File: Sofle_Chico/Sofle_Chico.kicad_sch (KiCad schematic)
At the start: 114 parts, among them J1 Conn_01x05, J2 MJ-4PP-9, J3 Conn_01x04, J4 Conn_01x04, J5 Conn_01x05, J6 Conn_01x05, J7 Conn_01x04, Q1 DMG2305UX, SW1 SW_PUSH, SW10 SW_PUSH, SW11 SW_PUSH, SW12 SW_PUSH, SW13 SW_PUSH, SW14 SW_PUSH, SW15 SW_PUSH, SW16 SW_PUSH, SW17 SW_PUSH, SW18 SW_PUSH, SW19 SW_PUSH, SW2 SW_PUSH, SW20 SW_PUSH, SW21 SW_PUSH, SW22 SW_PUSH, SW23 SW_PUSH, SW24 SW_PUSH, SW25 Rotary_Encoder_Switch-Device, SW26 SW_PUSH, SW27 SW_PUSH, SW28 SW_PUSH, SW29 SW_PUSH, SW3 SW_PUSH, SW30 SW_PUSH, SW4 SW_PUSH, SW5 SW_PUSH, SW6 SW_PUSH, SW7 SW_PUSH, SW8 SW_PUSH, SW9 SW_PUSH, U1 SN74AHCT1G125, U2 Pico

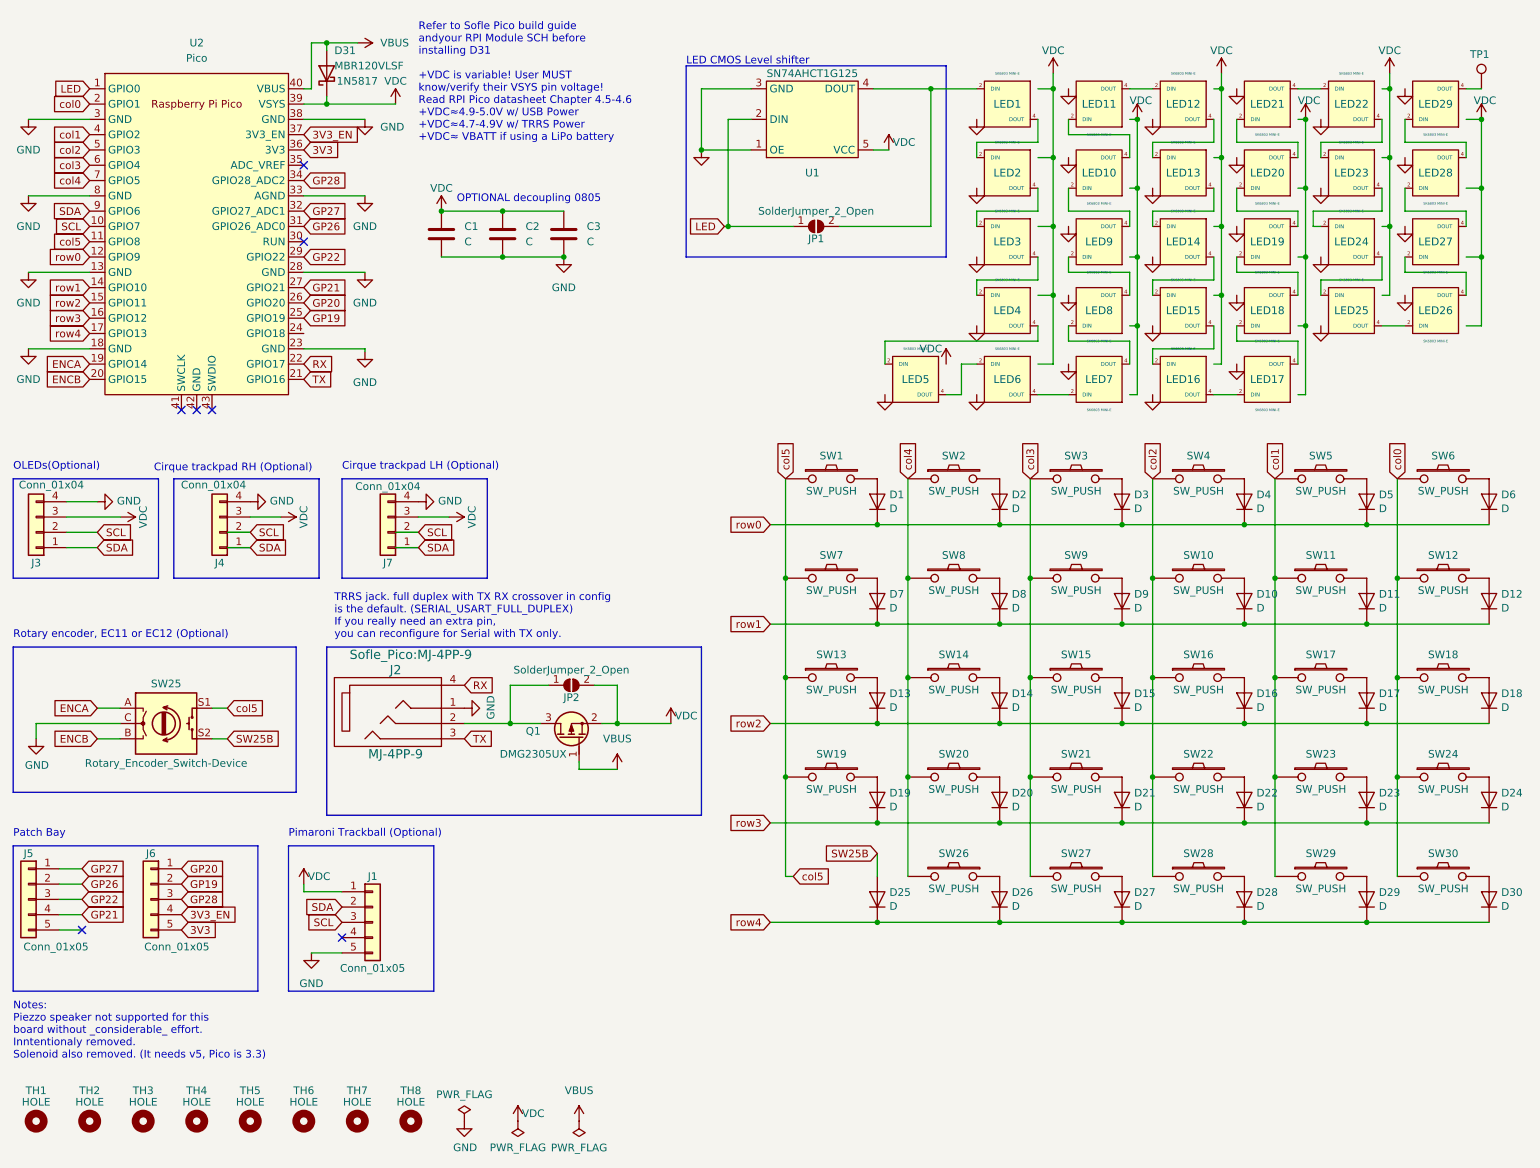
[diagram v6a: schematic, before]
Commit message: Completed routing and teardrops and cleared essential DRC errors
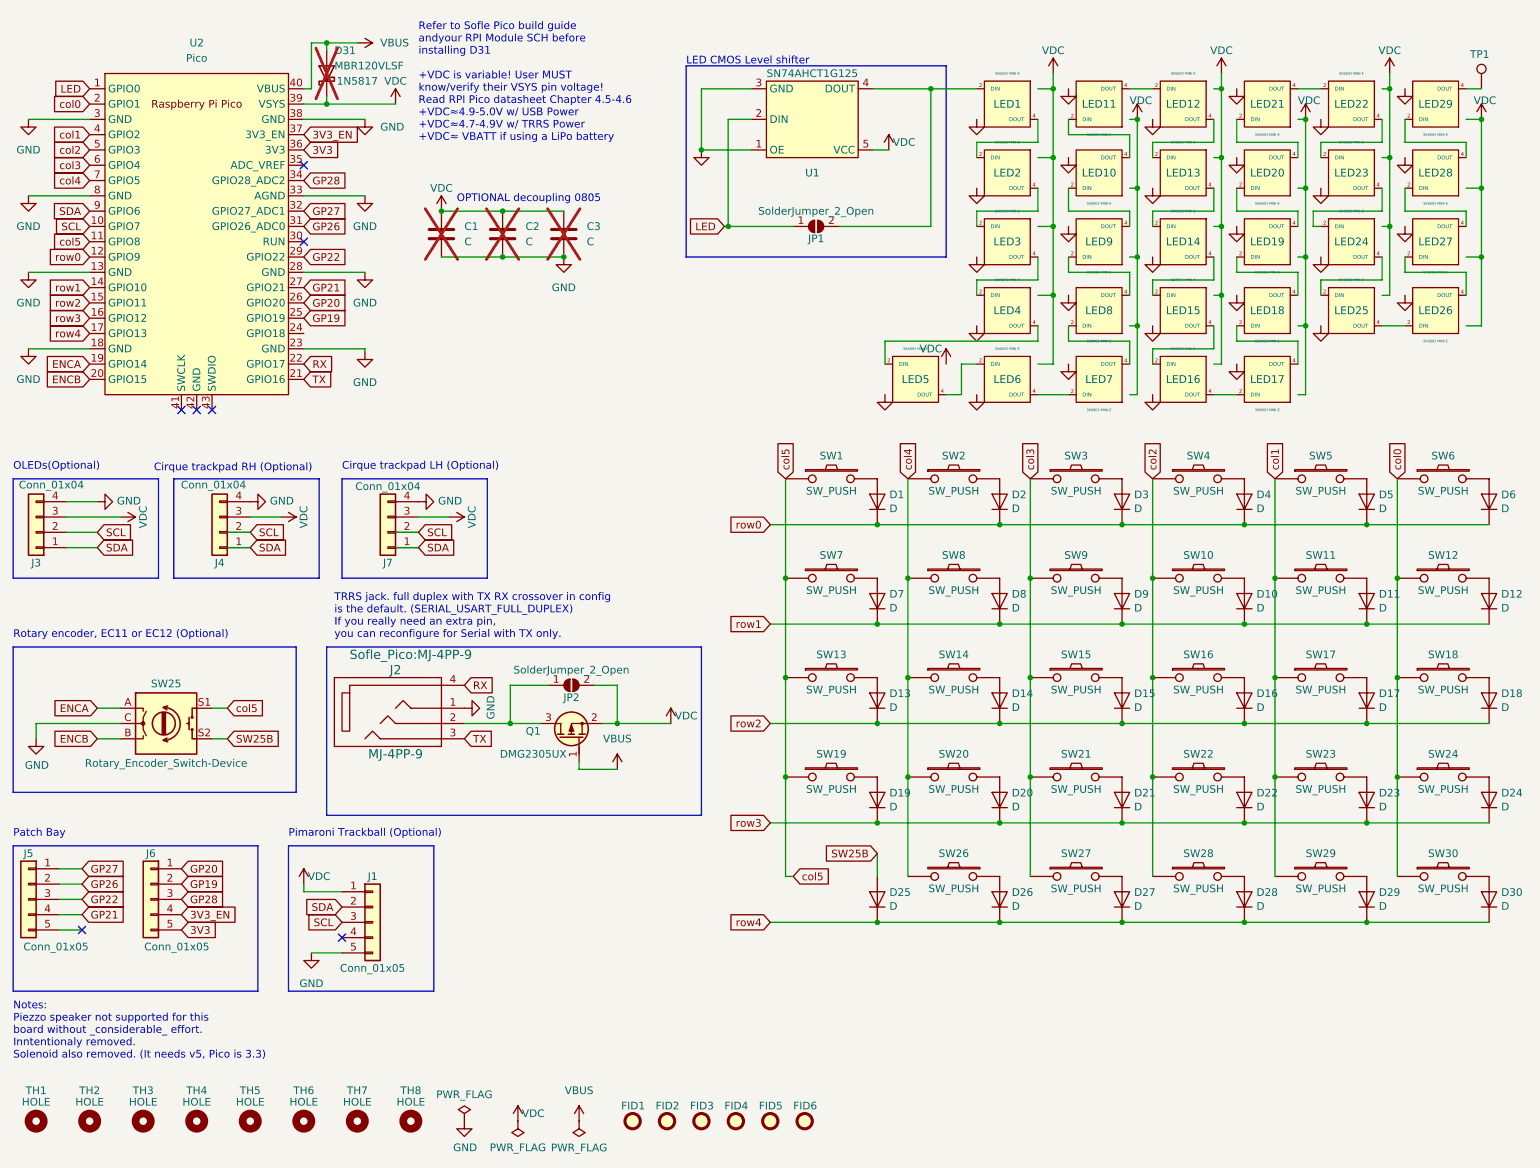
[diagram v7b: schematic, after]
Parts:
- added FID1, FID2, FID3, FID4, FID5, FID6: Fiducial, Fiducial:Fiducial_0.5mm_Mask1.5mm, symbol Mechanical:Fiducial
- C1, C2, C3, D31: now not fitted
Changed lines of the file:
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@@
+    )
+  )
+  (symbol (lib_id "Mechanical:Fiducial") (at 123.825 196.85 0) (unit 1)
+    (in_bom yes) (on_board yes) (dnp no)
+    (property "Reference" "FID2" (at 121.92 194.31 0)
+      (effects (font (size 1.27 1.27)) (justify left))
+    )
+    (property "Value" "Fiducial" (at 125.984 198.0621 0)
+      (effects (font (size 1.27 1.27)) (justify left) hide)
+    )
+    (property "Footprint" "Fiducial:Fiducial_0.5mm_Mask1.5mm" (at 123.825 196.85 0)
+      (effects (font (size 1.27 1.27)) hide)
+    )
+    (property "Datasheet" "~" (at 123.825 196.85 0)
+      (effects (font (size 1.27 1.27)) hide)
+    )
+    (instances
+      (project "Sofle_Chico"
+        (path "/06057b3a-55ab-4f4e-913e-2aeec5ff3587"
+          (reference "FID2") (unit 1)
+        )
+      )
     )
   )
@@
   )
   (symbol (lib_id "Device:C") (at 106.68 49.53 0) (unit 1)
-    (in_bom yes) (on_board yes) (dnp no) (fields_autoplaced)
+    (in_bom yes) (on_board yes) (dnp yes)
     (property "Reference" "C3" (at 110.49 48.26 0)
       (effects (font (size 1.27 1.27)) (justify left))
@@
         (path "/06057b3a-55ab-4f4e-913e-2aeec5ff3587"
           (reference "#PWR0113") (unit 1)
+        )
+      )
+    )
+  )
+  (symbol (lib_id "Mechanical:Fiducial") (at 146.685 196.85 0) (unit 1)
+    (in_bom yes) (on_board yes) (dnp no)
+    (property "Reference" "FID6" (at 144.78 194.31 0)
+      (effects (font (size 1.27 1.27)) (justify left))
+    )
+    (property "Value" "Fiducial" (at 148.844 198.0621 0)
+      (effects (font (size 1.27 1.27)) (justify left) hide)
+    )
+    (property "Footprint" "Fiducial:Fiducial_0.5mm_Mask1.5mm" (at 146.685 196.85 0)
+      (effects (font (size 1.27 1.27)) hide)
+    )
+    (property "Datasheet" "~" (at 146.685 196.85 0)
+      (effects (font (size 1.27 1.27)) hide)
+    )
+    (instances
+      (project "Sofle_Chico"
+        (path "/06057b3a-55ab-4f4e-913e-2aeec5ff3587"
+          (reference "FID6") (unit 1)
         )
       )
@@
     )
   )
+  (symbol (lib_id "Mechanical:Fiducial") (at 135.255 196.85 0) (unit 1)
+    (in_bom yes) (on_board yes) (dnp no)
+    (property "Reference" "FID4" (at 133.35 194.31 0)
+      (effects (font (size 1.27 1.27)) (justify left))
+    )
+    (property "Value" "Fiducial" (at 137.414 198.0621 0)
+      (effects (font (size 1.27 1.27)) (justify left) hide)
+    )
+    (property "Footprint" "Fiducial:Fiducial_0.5mm_Mask1.5mm" (at 135.255 196.85 0)
+      (effects (font (size 1.27 1.27)) hide)
+    )
+    (property "Datasheet" "~" (at 135.255 196.85 0)
+      (effects (font (size 1.27 1.27)) hide)
+    )
+    (instances
+      (project "Sofle_Chico"
+        (path "/06057b3a-55ab-4f4e-913e-2aeec5ff3587"
+          (reference "FID4") (unit 1)
+        )
+      )
+    )
+  )
   (symbol (lib_name "GND_3") (lib_id "power:GND") (at 73.66 43.18 0) (unit 1)
     (in_bom yes) (on_board yes) (dnp no) (fields_autoplaced)
@@
   )
   (symbol (lib_id "Diode:1N5817") (at 67.31 22.86 90) (unit 1)
-    (in_bom yes) (on_board yes) (dnp no)
+    (in_bom yes) (on_board yes) (dnp yes)
     (property "Reference" "D31" (at 68.58 19.05 90)
       (effects (font (size 1.27 1.27)) (justify right))
@@
     )
   )
+  (symbol (lib_id "Mechanical:Fiducial") (at 140.97 196.85 0) (unit 1)
+    (in_bom yes) (on_board yes) (dnp no)
+    (property "Reference" "FID5" (at 139.065 194.31 0)
+      (effects (font (size 1.27 1.27)) (justify left))
+    )
+    (property "Value" "Fiducial" (at 143.129 198.0621 0)
+      (effects (font (size 1.27 1.27)) (justify left) hide)
+    )
+    (property "Footprint" "Fiducial:Fiducial_0.5mm_Mask1.5mm" (at 140.97 196.85 0)
+      (effects (font (size 1.27 1.27)) hide)
+    )
+    (property "Datasheet" "~" (at 140.97 196.85 0)
+      (effects (font (size 1.27 1.27)) hide)
+    )
+    (instances
+      (project "Sofle_Chico"
+        (path "/06057b3a-55ab-4f4e-913e-2aeec5ff3587"
+          (reference "FID5") (unit 1)
+        )
+      )
+    )
+  )
   (symbol (lib_name "SK6803MINIE_V2_1") (lib_id "Sofle_Pico:SK6803MINIE_V2") (at 251.46 50.8 180) (unit 1)
     (in_bom yes) (on_board yes) (dnp no)
@@
   )
   (symbol (lib_id "Device:C") (at 86.36 49.53 0) (unit 1)
-    (in_bom yes) (on_board yes) (dnp no) (fields_autoplaced)
+    (in_bom yes) (on_board yes) (dnp yes) (fields_autoplaced)
     (property "Reference" "C1" (at 90.17 48.26 0)
       (effects (font (size 1.27 1.27)) (justify left))
@@
   )
   (symbol (lib_id "Device:C") (at 96.52 49.53 0) (unit 1)
-    (in_bom yes) (on_board yes) (dnp no) (fields_autoplaced)
+    (in_bom yes) (on_board yes) (dnp yes) (fields_autoplaced)
     (property "Reference" "C2" (at 100.33 48.26 0)
       (effects (font (size 1.27 1.27)) (justify left))
@@
     )
   )
+  (symbol (lib_id "Mechanical:Fiducial") (at 118.11 196.85 0) (unit 1)
+    (in_bom yes) (on_board yes) (dnp no)
+    (property "Reference" "FID1" (at 116.205 194.31 0)
+      (effects (font (size 1.27 1.27)) (justify left))
+    )
+    (property "Value" "Fiducial" (at 120.269 198.0621 0)
+      (effects (font (size 1.27 1.27)) (justify left) hide)
+    )
+    (property "Footprint" "Fiducial:Fiducial_0.5mm_Mask1.5mm" (at 118.11 196.85 0)
+      (effects (font (size 1.27 1.27)) hide)
+    )
+    (property "Datasheet" "~" (at 118.11 196.85 0)
+      (effects (font (size 1.27 1.27)) hide)
+    )
+    (instances
+      (project "Sofle_Chico"
+        (path "/06057b3a-55ab-4f4e-913e-2aeec5ff3587"
+          (reference "FID1") (unit 1)
+        )
+      )
+    )
+  )
   (symbol (lib_id "power:VDC") (at 201.93 30.48 0) (unit 1)
     (in_bom yes) (on_board yes) (dnp no)
@@
         )
       )
+    )
+  )
+  (symbol (lib_id "Mechanical:Fiducial") (at 129.54 196.85 0) (unit 1)
+    (in_bom yes) (on_board yes) (dnp no)
+    (property "Reference" "FID3" (at 127.635 194.31 0)
+      (effects (font (size 1.27 1.27)) (justify left))
+    )
+    (property "Value" "Fiducial" (at 131.699 198.0621 0)
+      (effects (font (size 1.27 1.27)) (justify left) hide)
+    )
+    (property "Footprint" "Fiducial:Fiducial_0.5mm_Mask1.5mm" (at 129.54 196.85 0)
+      (effects (font (size 1.27 1.27)) hide)
+    )
+    (property "Datasheet" "~" (at 129.54 196.85 0)
+      (effects (font (size 1.27 1.27)) hide)
+    )
+    (instances
+      (project "Sofle_Chico"
+        (path "/06057b3a-55ab-4f4e-913e-2aeec5ff3587"
+          (reference "FID3") (unit 1)
+        )
+      )
